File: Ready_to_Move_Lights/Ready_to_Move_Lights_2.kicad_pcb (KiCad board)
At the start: 2 copper layers, 76.2 x 76.2 mm, 34 parts, among them J1 PET-02-XX-X-VT-LC, K1 VORA1150-X017T, Q1 BC107, U1 LM393LVQDDFRQ1, U2 IPBT-102-H1-XX-S-RA, U3 NE555D, U4 IPBT-102-H1-XX-S-RA

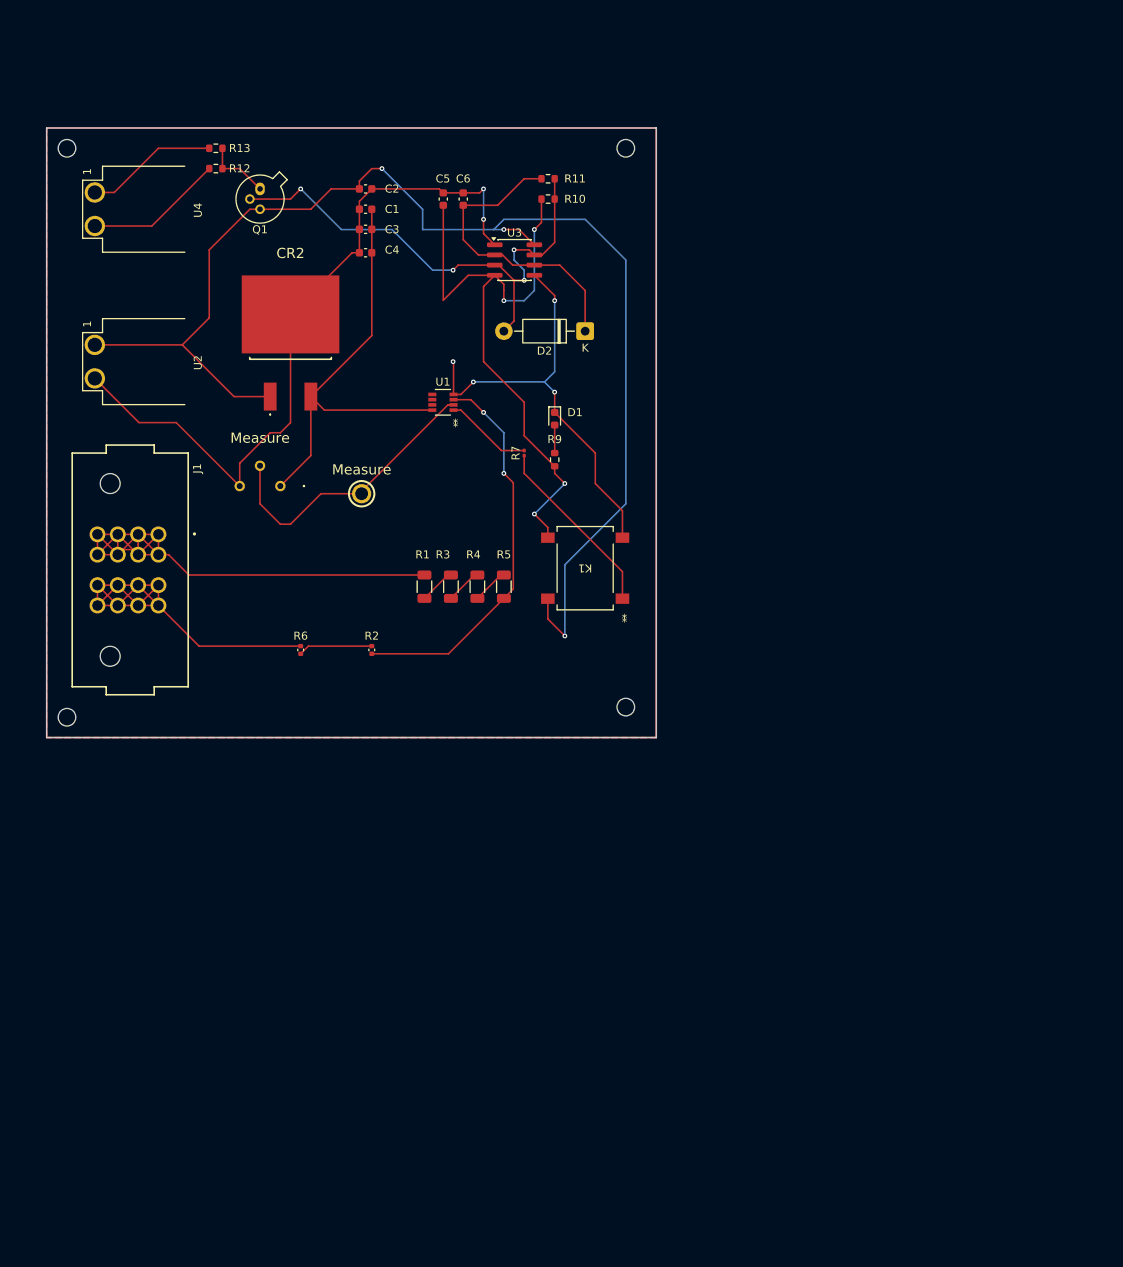
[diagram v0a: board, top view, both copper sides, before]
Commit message: Ready_to_Move_Lights
Updated ready to move lights schematic and pcb
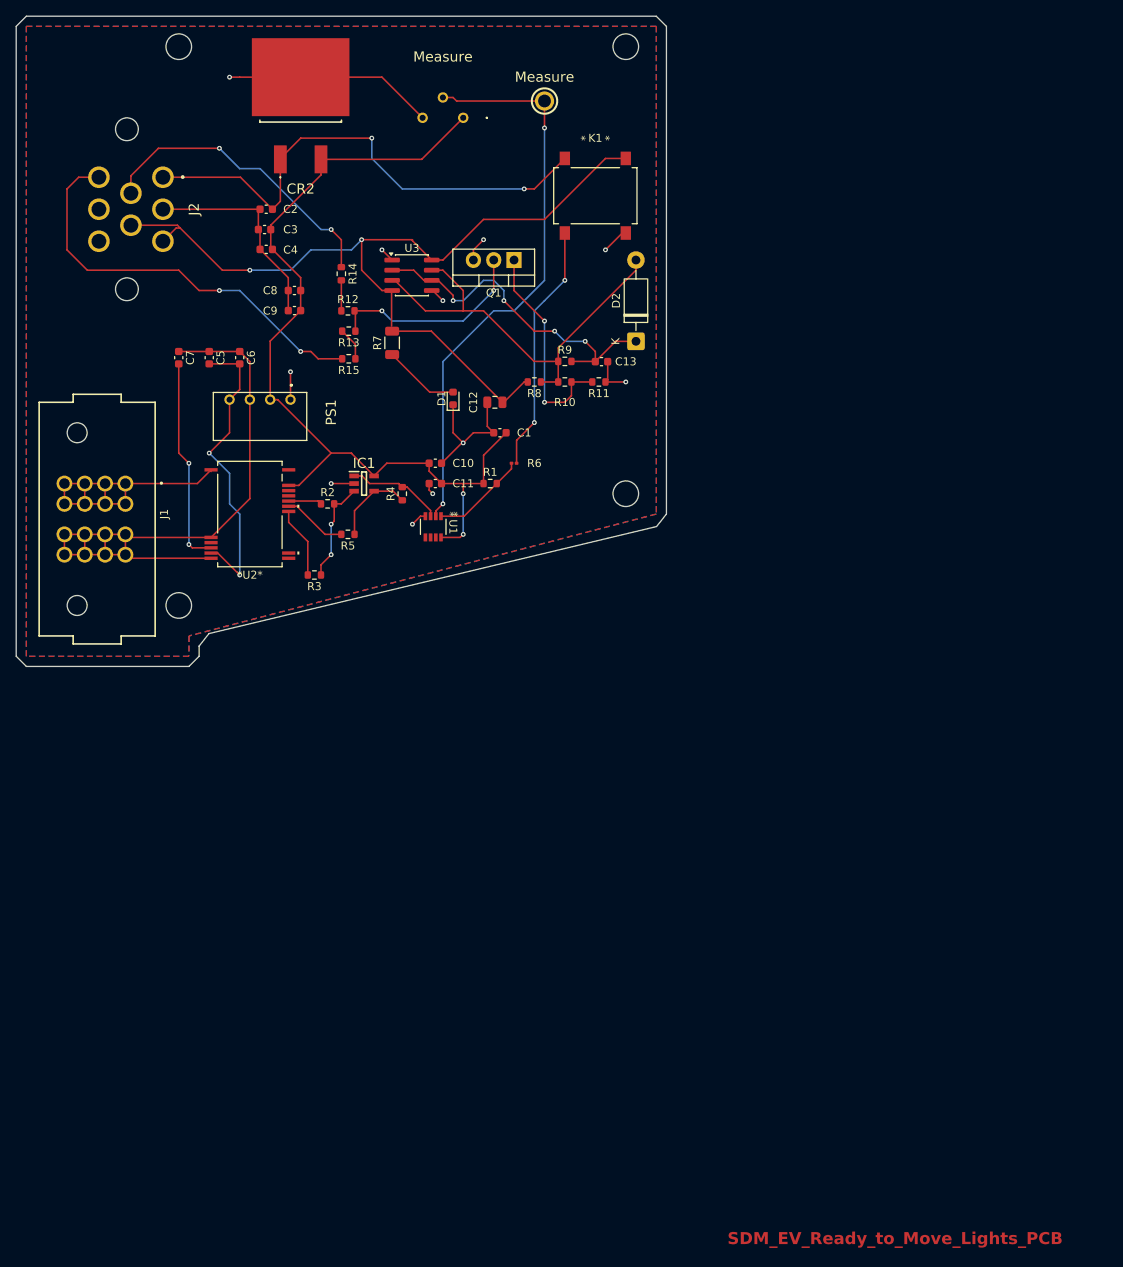
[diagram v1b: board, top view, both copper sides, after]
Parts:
- removed the ? at (174.0, 53.3)
- removed the ? at (174.0, 123.2)
- removed the ? at (104.1, 124.5)
- removed the ? at (104.1, 53.3)
- removed U4: IPBT-102-H1-XX-S-RA, Footprints:IPBT-102-H1-XX-S-RA
- added ?: , , F.Cu at (118.1, 40.6)
- added ?: , , F.Cu at (174.0, 40.6)
- added ?: , , F.Cu at (174.0, 96.5)
- added ?: , , F.Cu at (118.1, 110.5)
- added C10: 1uF, Capacitor_SMD:C_0603_1608Metric, F.Cu at (150.2, 92.7)
- added C11: 100nF, Capacitor_SMD:C_0603_1608Metric, F.Cu at (150.2, 95.2)
- added C12: 0.01uF, Capacitor_SMD:C_0805_2012Metric, F.Cu at (157.6, 85.1)
- added C13: 1.2uF, Capacitor_SMD:C_0603_1608Metric, F.Cu at (171.0, 80.0)
- added C7: 100pF, Capacitor_SMD:C_0603_1608Metric, F.Cu at (118.1, 79.5)
- added C8: 1uF, Capacitor_SMD:C_0603_1608Metric, F.Cu at (132.6, 71.1)
- added C9: 100nF, Capacitor_SMD:C_0603_1608Metric, F.Cu at (132.6, 73.6)
- added IC1: TLV2371QDBVRQ1, Footprints:SOT95P280X145-5N, F.Cu at (141.3, 95.2)
- added J2: 776280-1, SDM_MiscFootprint:776280-1, F.Cu at (100.3, 61.0)
- added PS1: TEA_1-0505, Footprints:TEA10505, F.Cu at (132.1, 84.8)
- added R14: 100, Resistor_SMD:R_0603_1608Metric, F.Cu at (138.4, 69.0)
- added R15: 100, Resistor_SMD:R_0603_1608Metric, F.Cu at (139.4, 79.7)
- added R8: 200k, Resistor_SMD:R_0603_1608Metric, F.Cu at (162.6, 82.5)
- C5: value 0.01uF -> 1uF
- C6: value 1.2uF -> 100nF
- D1: value LED -> RED LED
- Q1: value BC107 -> IRLZ44N; footprint Package_TO_SOT_THT:TO-18-3 -> Package_TO_SOT_THT:TO-220-3_Vertical
- R1: value 500K -> 200; footprint Resistor_SMD:R_1206_3216Metric -> Resistor_SMD:R_0603_1608Metric
- R10: value 200k -> 470
- R11: value 200k -> 10k
- R12, R13: value R -> 25
- R2: value 8.4K -> 10k; footprint SDM_MiscFootprint:C_0402_1005Metric -> Resistor_SMD:R_0603_1608Metric
- R3, R4: value 500K -> 50k; footprint Resistor_SMD:R_1206_3216Metric -> Resistor_SMD:R_0603_1608Metric
- R5: value 500K -> 10k; footprint Resistor_SMD:R_1206_3216Metric -> Resistor_SMD:R_0603_1608Metric
- R6: value 8.4K -> 1.2K; footprint SDM_MiscFootprint:C_0402_1005Metric -> Resistor_SMD:R_0201_0603Metric
- R7: value 1.2K -> 499; footprint Resistor_SMD:R_0201_0603Metric -> Resistor_SMD:R_1206_3216Metric
- R9: value R -> 200k
- U2: value IPBT-102-H1-XX-S-RA -> PAMC0381D10QDFXRQ1; footprint Footprints:IPBT-102-H1-XX-S-RA -> Footprints:SSOP15_DFX_TEX
- moved RED_TP1 54.1 mm to (163.8, 47.4)
- moved VR1 51.4 mm to (153.7, 49.5)
- moved K1 46.6 mm to (170.2, 59.3), turned to 90 degrees
- moved R6 35.4 mm to (160.0, 92.7), turned to 180 degrees
- moved C5 35.3 mm to (121.9, 79.5), turned to -90 degrees
- moved C6 34.3 mm to (125.7, 79.5), turned to -90 degrees
- moved Q1 33.0 mm to (160.0, 67.3), turned to 180 degrees
- moved C1 32.6 mm to (158.3, 88.9)
- moved CR2 29.7 mm to (133.3, 47.8)
- moved R13 28.3 mm to (139.4, 76.2)
- moved R11 26.2 mm to (170.6, 82.5)
- moved R12 24.3 mm to (139.3, 73.7), turned to 0 degrees
- moved R10 23.0 mm to (166.4, 82.5), turned to 0 degrees
- moved R7 21.5 mm to (144.8, 77.7)
- moved R5 20.6 mm to (139.3, 101.6), turned to 180 degrees
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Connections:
- C5 pad 1: Net-(U3-R) -> 02
- C5 pad 2: GND -> +5VDD
- C6 pad 1: Net-(D2-K) -> 02
- C6 pad 2: GND -> +5VDD
- K1 pad 3: Net-(U3-R) -> /Light1+
- Q1 pad 1: Net-(Q1-E) -> Net-(Q1-G)
- Q1 pad 2: Net-(D2-A) -> Net-(Q1-D)
- Q1 pad 3: /12V Master -> GND
- R1 pad 1: Net-(R1-Pad1) -> +5V
- R1 pad 2: 01 -> /V_IND
- R10 pad 2: Net-(U3-R) -> Net-(Q1-G)
- R11 pad 1: Net-(D2-A) -> GND
- R11 pad 2: Net-(D2-K) -> Net-(Q1-G)
- R12 pad 1: Net-(Q1-E) -> Net-(R12-Pad1)
- R12 pad 2: /Vout_for_light_2 -> Net-(Q1-D)
- R13 pad 1: Net-(Q1-E) -> Net-(Q1-D)
- R13 pad 2: /Vout_for_light_1 -> Net-(R13-Pad2)
- R2 pad 1: /V_DIV -> /OUT_P
- R2 pad 2: Net-(R2-Pad2) -> Net-(IC1-IN+)
- R3 pad 1: Net-(R3-Pad1) -> Net-(IC1-IN+)
- R3 pad 2: Net-(R1-Pad1) -> GND
- R4 pad 1: Net-(R4-Pad1) -> Net-(IC1-IN-)
- R4 pad 2: Net-(R3-Pad1) -> /V_OUT
- R5 pad 1: /V_DIV -> Net-(IC1-IN-)
- R5 pad 2: Net-(R4-Pad1) -> /OUT_N
- R6 pad 1: Net-(R2-Pad2) -> Net-(K1-Pad1)
- R6 pad 2: 02 -> /V_IND
- R7 pad 1: Net-(K1-Pad1) -> Net-(D1-A)
- R7 pad 2: /V_IND -> /Light1+
- R9 pad 1: Net-(D1-A) -> Net-(D2-A)
- R9 pad 2: Net-(U3-R) -> Net-(D2-K)
- U1 pad 3: /V_DIV -> /V_OUT
- U2 pad 1: /12V Master -> 01
- U2 pad 2: GND -> 02
- U3 pad 4: Net-(U3-R) -> /Light1+
- U3 pad 8: /12V Master -> /Light1+
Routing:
- net /Light1+: track 0.00 -> 109.8 mm, vias 0 -> 2
- net /12V Master: track 163.6 -> 64.4 mm, vias 3 -> 2
- net Net-(U3-R): track 79.3 -> 0.00 mm, vias 4 -> 0
- net +5V: track 55.2 -> 112.4 mm, vias 0 -> 2
- net /Light2GND: track 0.00 -> 52.3 mm, vias 0 -> 2
- net /V_DIV: track 49.1 -> 0.00 mm, vias 2 -> 0
- net 01: track 81.8 -> 37.0 mm
- net GND: track 145.9 -> 104.4 mm, vias 6 -> 11
- net +5VDD: track 0.00 -> 38.1 mm, vias 0 -> 2
- net /Light1GND: track 0.00 -> 38.1 mm, vias 0 -> 2
- net /V_LOW_REF: track 36.4 -> 71.9 mm, vias 0 -> 2
- net Net-(Q1-G): track 0.00 -> 27.4 mm, vias 0 -> 2
- net Net-(U2-SNSP): track 0.00 -> 26.0 mm, vias 0 -> 2
- net Net-(Q1-D): track 0.00 -> 25.9 mm, vias 0 -> 2
- net 02: track 61.8 -> 81.0 mm
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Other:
- board size 76.2 x 76.2 mm -> 81.3 x 81.3 mm
- board text added: "SDM_EV_Ready_to_Move_Lights_PCB"

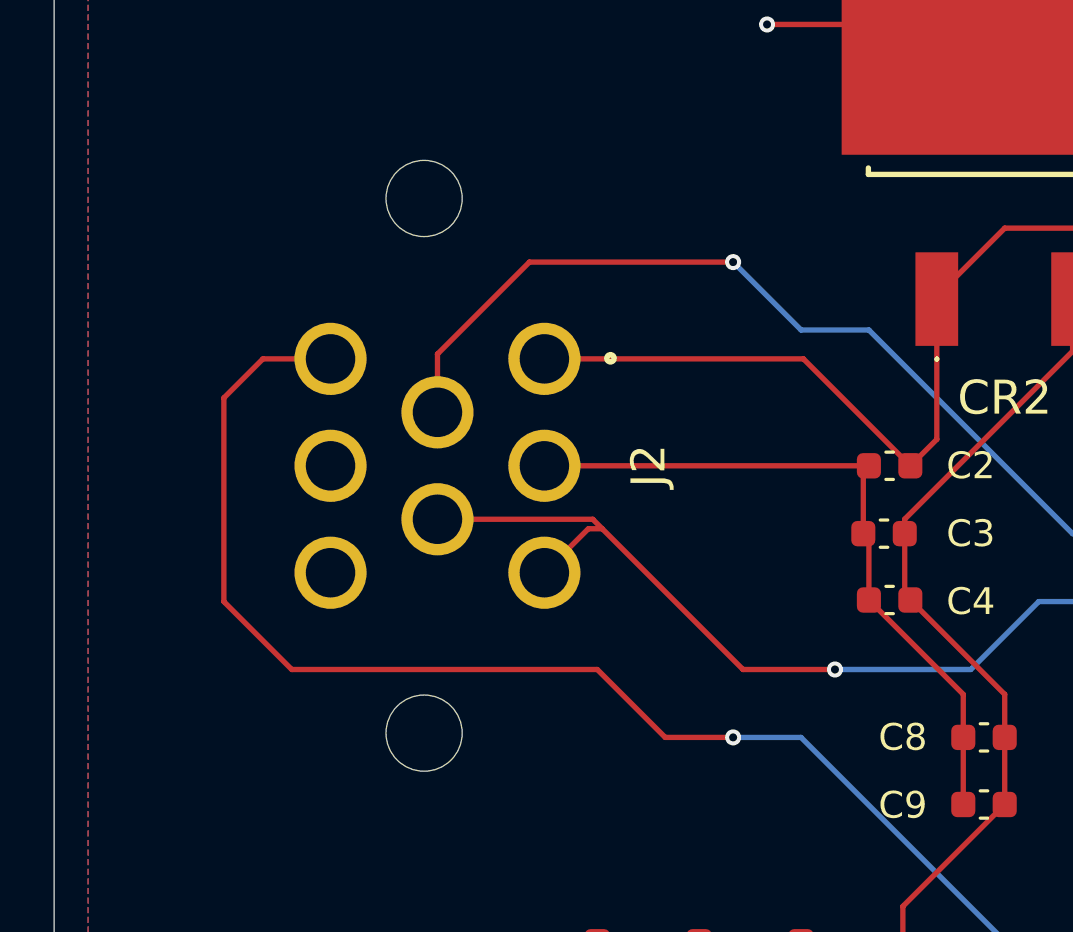
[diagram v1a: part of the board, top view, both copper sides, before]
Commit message: Fixed Ready_to_Move_Lights
Noticed this morning i didnt pay attention and messed up the connector placement
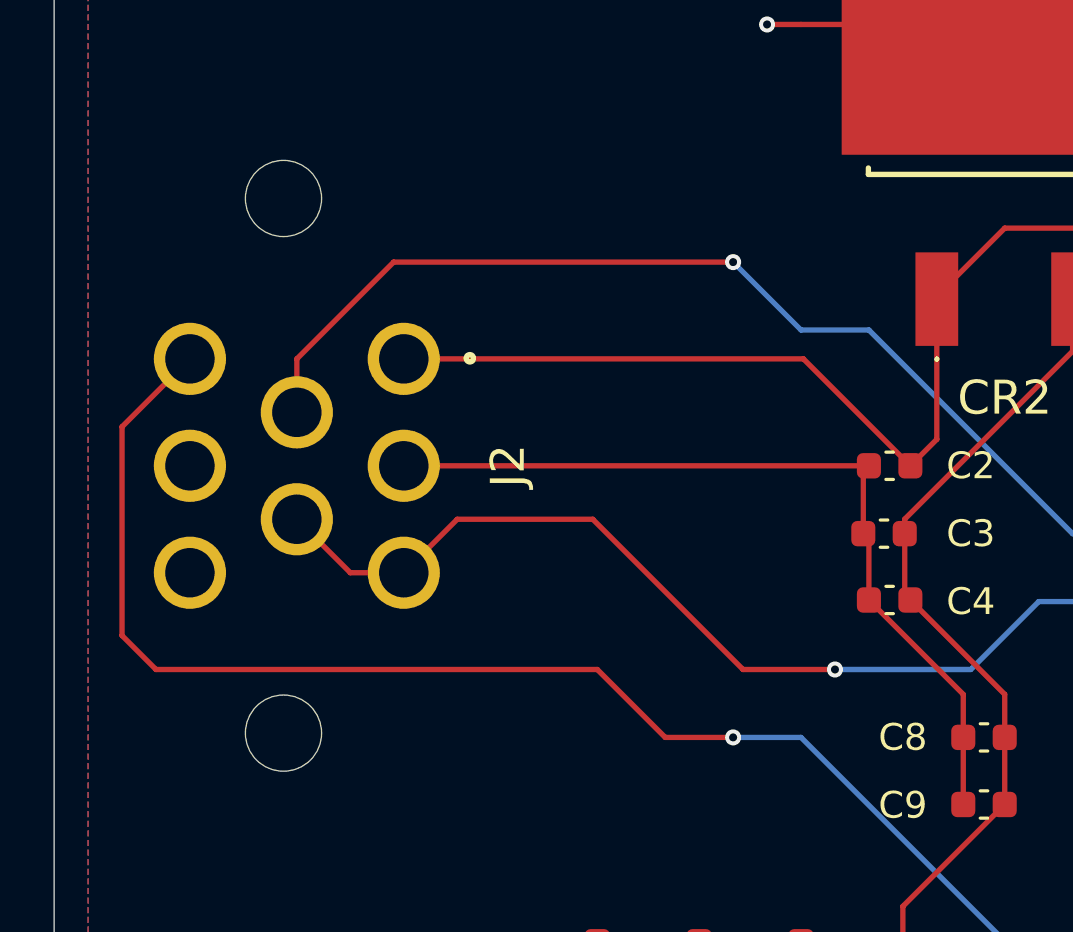
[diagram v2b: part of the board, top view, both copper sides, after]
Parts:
- moved J2 5.26 mm to (95.1, 61.0)
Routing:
- net GND: track 104.4 -> 109.7 mm
- net /12V Master: track 64.4 -> 69.7 mm
- net /Light1GND: track 38.1 -> 43.2 mm
- net /Light1+: track 109.8 -> 113.9 mm
- net /Light2GND: track 52.3 -> 54.7 mm
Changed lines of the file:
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@@
 	(footprint "SDM_MiscFootprint:776280-1"
 		(layer "F.Cu")
-		(at 100.33 60.96 -90)
+		(at 95.07 60.96 -90)
 		(descr "776280-1")
 		(tags "Connector")
@@
 	)
 	(segment
-		(start 116.13 60.96)
-		(end 128.27 60.96)
-		(width 0.2)
-		(layer "F.Cu")
-		(net 1)
-	)
-	(segment
 		(start 148.59 49.53)
 		(end 143.51 44.45)
@@
 	)
 	(segment
+		(start 110.87 60.96)
+		(end 128.27 60.96)
+		(width 0.2)
+		(layer "F.Cu")
+		(net 1)
+	)
+	(segment
 		(start 131.8514 100.1014)
 		(end 134.24 102.49)
@@
 	(segment
 		(start 125.82 56.96)
-		(end 129.82 60.96)
-		(width 0.2)
-		(layer "F.Cu")
-		(net 3)
-	)
-	(segment
-		(start 116.13 56.96)
-		(end 125.82 56.96)
+		(end 110.87 56.96)
 		(width 0.2)
 		(layer "F.Cu")
@@
 		(net 3)
 	)
+	(segment
+		(start 129.82 60.96)
+		(end 125.82 56.96)
+		(width 0.2)
+		(layer "F.Cu")
+		(net 3)
+	)
 	(via
 		(at 161.29 58.42)
@@
 	)
 	(segment
+		(start 106.87 62.96)
+		(end 108.87 64.96)
+		(width 0.2)
+		(layer "F.Cu")
+		(net 7)
+	)
+	(segment
 		(start 147.32 64.9)
 		(end 149.73 67.31)
@@
 	)
 	(segment
-		(start 118.295 63.315)
+		(start 127 68.58)
 		(end 123.56 68.58)
 		(width 0.2)
@@
 	)
 	(segment
-		(start 117.94 62.96)
-		(end 118.295 63.315)
+		(start 140.97 68.58)
+		(end 140.97 64.77)
 		(width 0.2)
 		(layer "F.Cu")
@@
 	)
 	(segment
-		(start 112.13 62.96)
+		(start 123.56 68.58)
 		(end 117.94 62.96)
 		(width 0.2)
@@
 	)
 	(segment
-		(start 140.97 68.58)
-		(end 140.97 64.77)
+		(start 149.685 76.2)
+		(end 144.78 76.2)
 		(width 0.2)
 		(layer "F.Cu")
@@
 	)
 	(segment
-		(start 149.685 76.2)
-		(end 144.78 76.2)
+		(start 161.29 82.55)
+		(end 161.735 82.55)
 		(width 0.2)
 		(layer "F.Cu")
@@
 	)
 	(segment
-		(start 161.29 82.55)
-		(end 161.735 82.55)
+		(start 117.94 62.96)
+		(end 112.87 62.96)
 		(width 0.2)
 		(layer "F.Cu")
@@
 	)
 	(segment
-		(start 123.56 68.58)
-		(end 127 68.58)
-		(width 0.2)
-		(layer "F.Cu")
-		(net 7)
-	)
-	(segment
 		(start 144.78 71.12)
 		(end 143.51 71.12)
@@
 	)
 	(segment
-		(start 116.13 64.96)
-		(end 117.775 63.315)
+		(start 112.87 62.96)
+		(end 110.87 64.96)
 		(width 0.2)
 		(layer "F.Cu")
@@
 	)
 	(segment
-		(start 171.45 54.61)
-		(end 163.83 62.23)
+		(start 108.87 64.96)
+		(end 110.87 64.96)
 		(width 0.2)
 		(layer "F.Cu")
@@
 	)
 	(segment
-		(start 117.775 63.315)
-		(end 118.295 63.315)
+		(start 171.45 54.61)
+		(end 163.83 62.23)
 		(width 0.2)
 		(layer "F.Cu")
@@
 	)
 	(segment
-		(start 104.14 58.42)
-		(end 105.6 56.96)
-		(width 0.2)
-		(layer "F.Cu")
-		(net 16)
-	)
-	(segment
-		(start 123.19 71.12)
-		(end 120.65 71.12)
+		(start 138.5385 79.654501)
+		(end 135.534501 79.654501)
 		(width 0.2)
 		(layer "F.Cu")
@@
 	)
 	(segment
-		(start 106.68 68.58)
-		(end 104.14 66.04)
+		(start 102.87 56.96)
+		(end 100.33 59.5)
 		(width 0.2)
 		(layer "F.Cu")
@@
 	)
 	(segment
-		(start 138.5385 79.654501)
-		(end 135.534501 79.654501)
+		(start 101.6 68.58)
+		(end 118.11 68.58)
 		(width 0.2)
 		(layer "F.Cu")
@@
 	(segment
 		(start 118.11 68.58)
-		(end 106.68 68.58)
+		(end 120.65 71.12)
 		(width 0.2)
 		(layer "F.Cu")
@@
 	)
 	(segment
-		(start 120.65 71.12)
-		(end 118.11 68.58)
+		(start 100.33 59.5)
+		(end 100.33 67.31)
 		(width 0.2)
 		(layer "F.Cu")
@@
 	)
 	(segment
-		(start 104.14 66.04)
-		(end 104.14 58.42)
+		(start 134.62 78.74)
+		(end 135.534501 79.654501)
 		(width 0.2)
 		(layer "F.Cu")
@@
 	)
 	(segment
-		(start 134.62 78.74)
-		(end 135.534501 79.654501)
+		(start 133.35 78.74)
+		(end 134.62 78.74)
 		(width 0.2)
 		(layer "F.Cu")
@@
 	)
 	(segment
-		(start 133.35 78.74)
-		(end 134.62 78.74)
+		(start 120.65 71.12)
+		(end 123.19 71.12)
 		(width 0.2)
 		(layer "F.Cu")
@@
 	)
 	(segment
-		(start 105.6 56.96)
-		(end 108.13 56.96)
+		(start 100.33 67.31)
+		(end 101.6 68.58)
 		(width 0.2)
 		(layer "F.Cu")
@@
 	)
 	(segment
-		(start 112.13 56.78)
-		(end 112.13 58.96)
+		(start 123.19 53.34)
+		(end 110.49 53.34)
 		(width 0.2)
 		(layer "F.Cu")
@@
 	)
 	(segment
-		(start 123.19 53.34)
-		(end 115.57 53.34)
+		(start 106.87 56.96)
+		(end 106.87 58.96)
 		(width 0.2)
 		(layer "F.Cu")
@@
 	)
 	(segment
-		(start 115.57 53.34)
-		(end 112.13 56.78)
+		(start 110.49 53.34)
+		(end 106.87 56.96)
 		(width 0.2)
 		(layer "F.Cu")
